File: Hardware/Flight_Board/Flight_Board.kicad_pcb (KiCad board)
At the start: 2 copper layers, 50.8 x 101.6 mm, 128 parts, among them J1 Conn_01x04, J2 Conn_01x08, J3 Conn_01x04, J4 Conn_01x06, J5 MEM2067-02-180-00-A_REVB, SW1 SW_Push, U1 FT5HN, U2 STM32F411RCTx, U3 ADXL375, U4 BMP390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

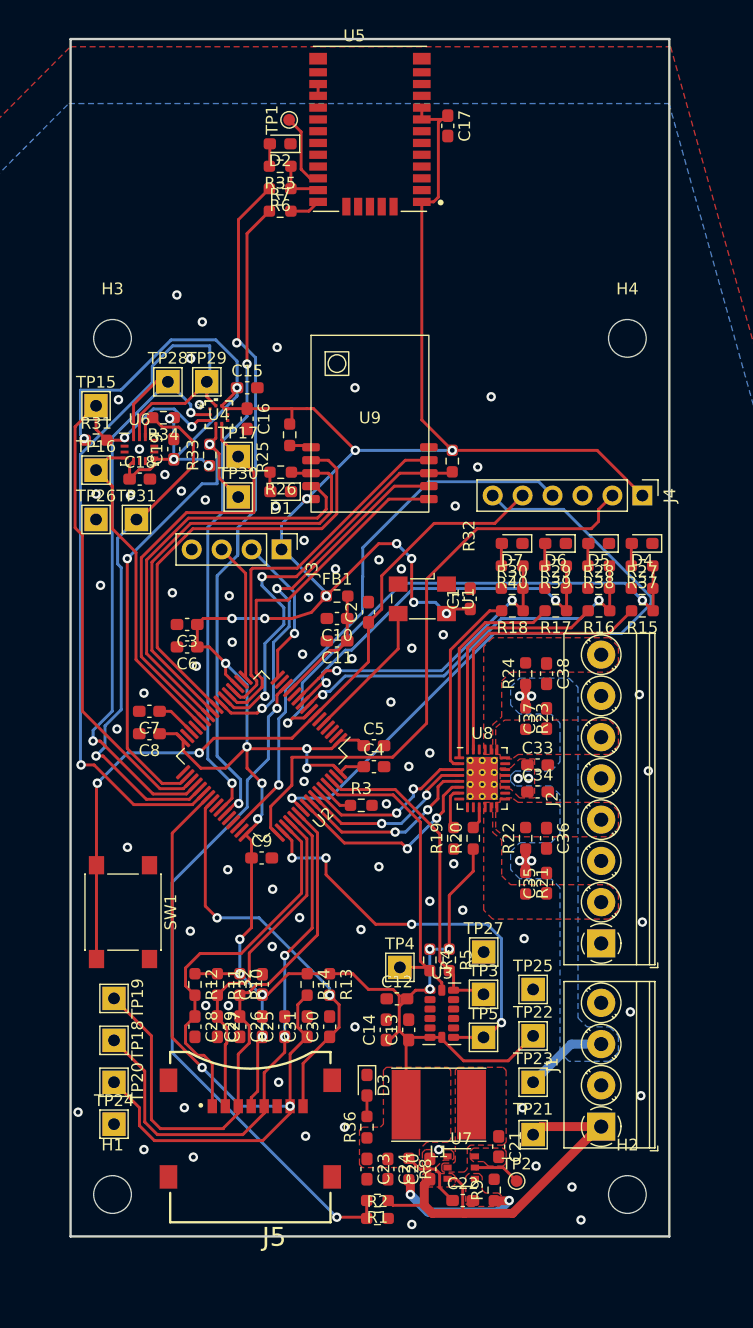
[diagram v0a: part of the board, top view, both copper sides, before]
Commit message: begin fixing silkscreen
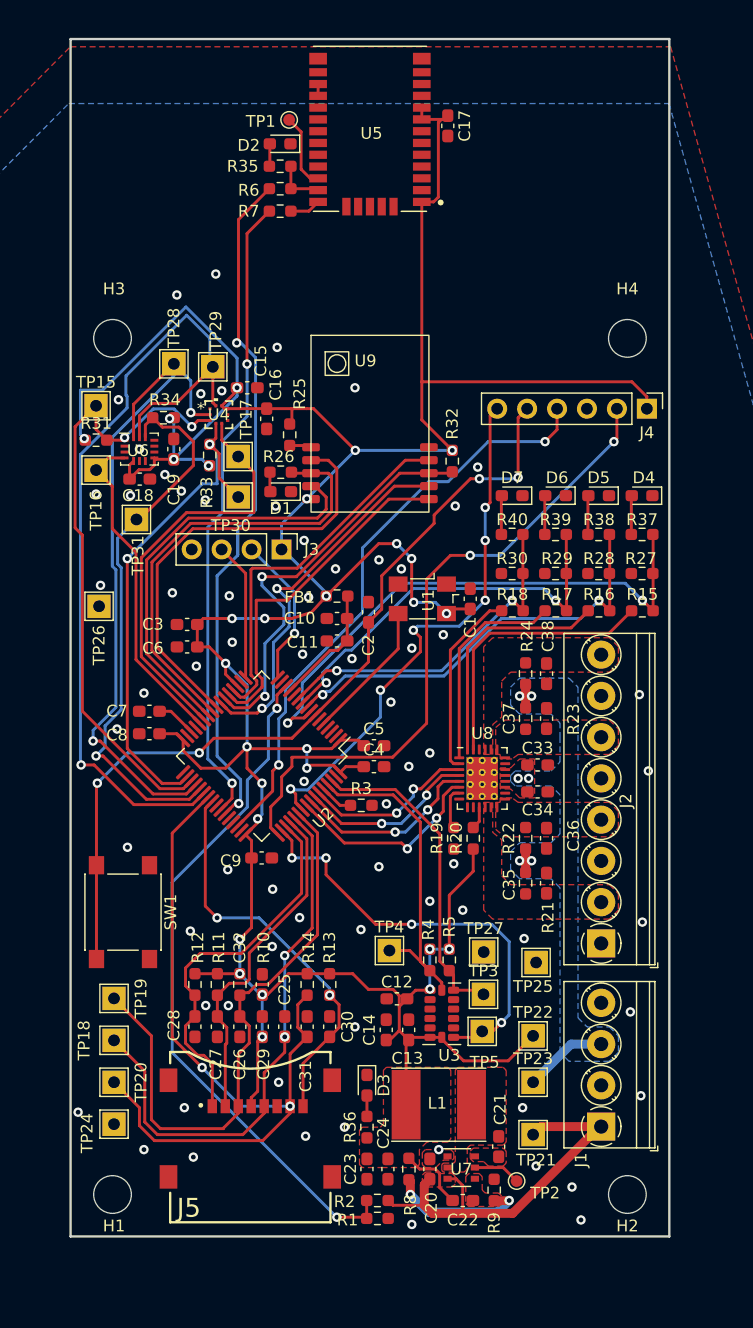
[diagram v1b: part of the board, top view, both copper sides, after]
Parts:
- moved J4 7.38 mm to (158.8, 69.8)
- moved TP26 7.37 mm to (112.3, 86.6)
- moved D4 4.05 mm to (158.3, 77.2)
- moved D5 4.05 mm to (154.7, 77.2)
- moved D6 4.05 mm to (151.0, 77.2)
- moved D7 4.05 mm to (147.3, 77.2)
- moved R37 2.67 mm to (158.3, 80.5)
- moved R38 2.67 mm to (154.7, 80.5)
- moved R39 2.67 mm to (151.0, 80.5)
- moved R40 2.67 mm to (147.3, 80.5)
- moved TP25 2.30 mm to (149.4, 116.8)
- moved TP4 1.68 mm to (136.9, 115.8)
- moved C16 1.66 mm to (126.5, 70.7)
- moved TP28 1.61 mm to (118.6, 66.0)
- moved TP29 1.37 mm to (121.9, 66.3)
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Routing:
- net /Microcontroller/SWO: track 56.3 -> 45.3 mm, vias 1 -> 6
- net /Microcontroller/NRST: track 64.8 -> 71.6 mm, vias 2 -> 4
- net +3.3V: track 308.4 -> 313.8 mm
- net /Barometer/MOSI: track 55.6 -> 60.1 mm
- net /Microcontroller/SWCLK: track 51.7 -> 56.0 mm, vias 0 -> 2
- net /Barometer/SCK: track 68.4 -> 72.7 mm
- net /Microcontroller/SWDIO: track 47.1 -> 50.5 mm, vias 1 -> 2
- net /Current Switch/EN3: track 31.9 -> 34.6 mm
- net /Current Switch/EN1: track 44.4 -> 47.1 mm
- net /Current Switch/EN4: track 26.7 -> 29.4 mm
- net /Current Switch/EN2: track 33.6 -> 36.3 mm
- net /Accelerometer/SCL: track 26.8 -> 28.3 mm
- net Net-(D7-A): track 1.95 -> 3.31 mm
- net Net-(D6-A): track 1.95 -> 3.31 mm
- net Net-(D5-A): track 1.95 -> 3.31 mm
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
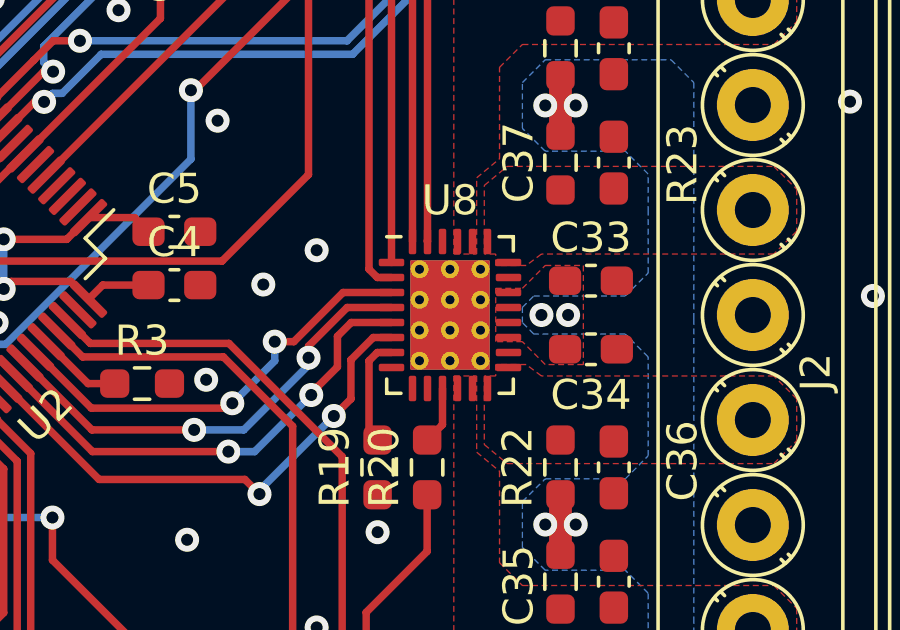
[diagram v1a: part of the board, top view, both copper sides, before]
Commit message: edit pcb with new footprint
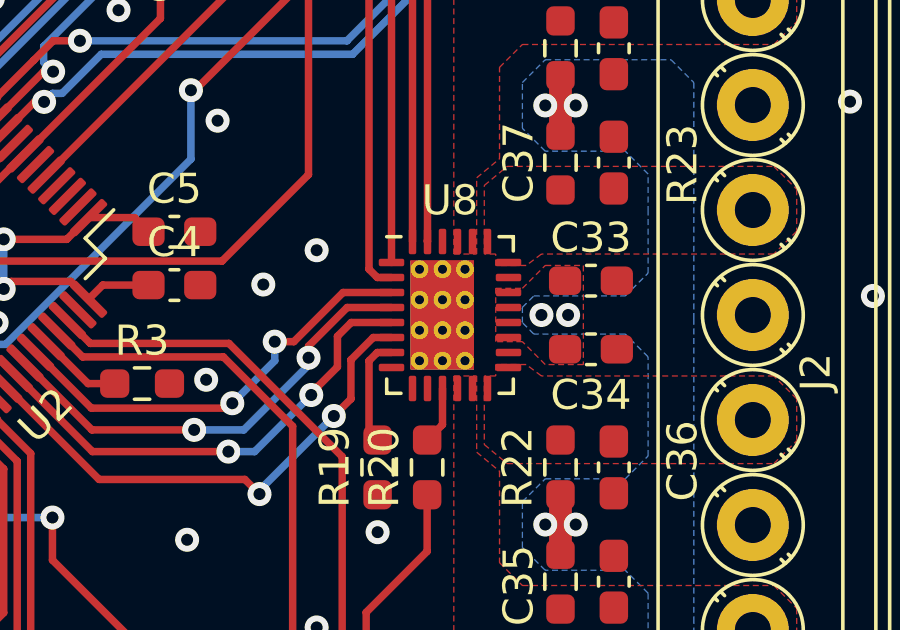
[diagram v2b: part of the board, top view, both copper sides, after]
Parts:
- U8: footprint Package_DFN_QFN:QFN-28-1EP_4x5mm_P0.5mm_EP2.65x3.65mm_ThermalVias -> Project:TPS274160A
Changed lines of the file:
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@@
     )
   )
-  (footprint "Package_DFN_QFN:QFN-28-1EP_4x5mm_P0.5mm_EP2.65x3.65mm_ThermalVias" (layer "F.Cu")
+  (footprint "Project:TPS274160A" (layer "F.Cu")
     (at 144.78 101.219)
     (descr "QFN, 28 Pin (http://www.analog.com/media/en/technical-documentation/data-sheets/3555fe.pdf#page=32), generated with kicad-footprint-generator ipc_noLead_generator.py")
@@
     (fp_line (start 2 2.5) (end -2 2.5)
       (stroke (width 0.1) (type solid)) (layer "F.Fab"))
-    (pad "" smd roundrect (at -0.66 -1.22) (size 1.07 0.98) (layers "F.Paste") (roundrect_rratio 0.25))
-    (pad "" smd roundrect (at -0.66 0) (size 1.07 0.98) (layers "F.Paste") (roundrect_rratio 0.25))
-    (pad "" smd roundrect (at -0.66 1.22) (size 1.07 0.98) (layers "F.Paste") (roundrect_rratio 0.25))
-    (pad "" smd roundrect (at 0.66 -1.22) (size 1.07 0.98) (layers "F.Paste") (roundrect_rratio 0.25))
-    (pad "" smd roundrect (at 0.66 0) (size 1.07 0.98) (layers "F.Paste") (roundrect_rratio 0.25))
-    (pad "" smd roundrect (at 0.66 1.22) (size 1.07 0.98) (layers "F.Paste") (roundrect_rratio 0.25))
     (pad "1" smd roundrect (at -1.95 -1.75) (size 0.85 0.25) (layers "F.Cu" "F.Paste" "F.Mask") (roundrect_rratio 0.25)
       (net 46 "Net-(U8-EN3)") (pinfunction "EN3") (pintype "input"))
@@
     (pad "28" smd roundrect (at -1.25 -2.45) (size 0.25 0.85) (layers "F.Cu" "F.Paste" "F.Mask") (roundrect_rratio 0.25)
       (net 44 "Net-(U8-EN2)") (pinfunction "EN2") (pintype "input"))
-    (pad "29" thru_hole circle (at -1.016 -1.524) (size 0.6 0.6) (drill 0.3) (layers "*.Cu")
+    (pad "29" thru_hole circle (at -1.016 -1.523) (size 0.6 0.6) (drill 0.3) (layers "*.Cu")
       (net 2 "GND") (pinfunction "PAD") (pintype "power_in"))
-    (pad "29" thru_hole circle (at -1.016 -0.508) (size 0.6 0.6) (drill 0.3) (layers "*.Cu")
+    (pad "29" thru_hole circle (at -1.016 -0.507) (size 0.6 0.6) (drill 0.3) (layers "*.Cu")
       (net 2 "GND") (pinfunction "PAD") (pintype "power_in"))
-    (pad "29" thru_hole circle (at -1.016 0.508) (size 0.6 0.6) (drill 0.3) (layers "*.Cu")
+    (pad "29" thru_hole circle (at -1.016 0.509) (size 0.6 0.6) (drill 0.3) (layers "*.Cu")
       (net 2 "GND") (pinfunction "PAD") (pintype "power_in"))
-    (pad "29" thru_hole circle (at -1.016 1.524) (size 0.6 0.6) (drill 0.3) (layers "*.Cu")
+    (pad "29" thru_hole circle (at -1.016 1.525) (size 0.6 0.6) (drill 0.3) (layers "*.Cu")
       (net 2 "GND") (pinfunction "PAD") (pintype "power_in"))
-    (pad "29" thru_hole circle (at 0 -1.524) (size 0.6 0.6) (drill 0.3) (layers "*.Cu")
+    (pad "29" smd rect (at -0.2625 0) (size 2.125 3.65) (layers "F.Cu" "F.Mask")
       (net 2 "GND") (pinfunction "PAD") (pintype "power_in"))
-    (pad "29" thru_hole circle (at 0 -0.508) (size 0.6 0.6) (drill 0.3) (layers "*.Cu")
+    (pad "29" smd rect (at -0.2625 0.001) (size 2.125 3.648) (layers "B.Cu")
       (net 2 "GND") (pinfunction "PAD") (pintype "power_in"))
-    (pad "29" smd rect (at 0 0) (size 2.65 3.65) (layers "F.Cu" "F.Mask")
+    (pad "29" thru_hole circle (at -0.25 -1.525) (size 0.6 0.6) (drill 0.3) (layers "*.Cu")
       (net 2 "GND") (pinfunction "PAD") (pintype "power_in"))
-    (pad "29" smd rect (at 0 0) (size 2.65 3.65) (layers "B.Cu")
+    (pad "29" thru_hole circle (at -0.25 -0.507) (size 0.6 0.6) (drill 0.3) (layers "*.Cu")
       (net 2 "GND") (pinfunction "PAD") (pintype "power_in"))
-    (pad "29" thru_hole circle (at 0 0.508) (size 0.6 0.6) (drill 0.3) (layers "*.Cu")
+    (pad "29" thru_hole circle (at -0.25 0.509) (size 0.6 0.6) (drill 0.3) (layers "*.Cu")
       (net 2 "GND") (pinfunction "PAD") (pintype "power_in"))
-    (pad "29" thru_hole circle (at 0 1.524) (size 0.6 0.6) (drill 0.3) (layers "*.Cu")
+    (pad "29" thru_hole circle (at -0.25 1.525) (size 0.6 0.6) (drill 0.3) (layers "*.Cu")
       (net 2 "GND") (pinfunction "PAD") (pintype "power_in"))
-    (pad "29" thru_hole circle (at 1.016 -1.524) (size 0.6 0.6) (drill 0.3) (layers "*.Cu")
+    (pad "29" thru_hole circle (at 0.5 -1.525) (size 0.6 0.6) (drill 0.3) (layers "*.Cu")
       (net 2 "GND") (pinfunction "PAD") (pintype "power_in"))
-    (pad "29" thru_hole circle (at 1.016 -0.508) (size 0.6 0.6) (drill 0.3) (layers "*.Cu")
+    (pad "29" thru_hole circle (at 0.5 -0.507) (size 0.6 0.6) (drill 0.3) (layers "*.Cu")
       (net 2 "GND") (pinfunction "PAD") (pintype "power_in"))
-    (pad "29" thru_hole circle (at 1.016 0.508) (size 0.6 0.6) (drill 0.3) (layers "*.Cu")
+    (pad "29" thru_hole circle (at 0.5 0.509) (size 0.6 0.6) (drill 0.3) (layers "*.Cu")
       (net 2 "GND") (pinfunction "PAD") (pintype "power_in"))
-    (pad "29" thru_hole circle (at 1.016 1.524) (size 0.6 0.6) (drill 0.3) (layers "*.Cu")
+    (pad "29" thru_hole circle (at 0.5 1.525) (size 0.6 0.6) (drill 0.3) (layers "*.Cu")
       (net 2 "GND") (pinfunction "PAD") (pintype "power_in"))
     (model "${KICAD6_3DMODEL_DIR}/Package_DFN_QFN.3dshapes/QFN-28-1EP_4x5mm_P0.5mm_EP2.65x3.65mm.wrl"

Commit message: update silkscreen
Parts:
- moved TP16 2.92 mm to (112.0, 78.0)
- moved TP29 1.02 mm to (121.9, 65.3)
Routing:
- net /Barometer/SCK: track 72.7 -> 73.7 mm
- net +3.3V: track 313.8 -> 314.7 mm
- net /IMU/INT1: track 28.0 -> 27.2 mm
- net GND: vias 70 -> 69
